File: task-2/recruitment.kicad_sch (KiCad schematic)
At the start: 0 parts

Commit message: Schema con partitori per le soglie, comparatori per i sensori e alimentazione del Lm393
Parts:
- added R1: 9.1k, symbol Device:R
- added R2: 4.7k, symbol Device:R
- added R3: 13k, symbol Device:R
- added R4: 15k, symbol Device:R
- added U1: LM393, symbol Comparator:LM393
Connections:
- new net BRAKE_SENS: U1.3 (+)
- new net CURR_SENS: U1.5 (+)
- new net GND: R2.2, R4.2, U1.4 (V-)
- new net VIN: U1.8 (V+)
- new net V_refBrake: R1.2, R2.1, U1.2 (-)
- new net V_refCurrent: R3.2, R4.1, U1.6 (-)

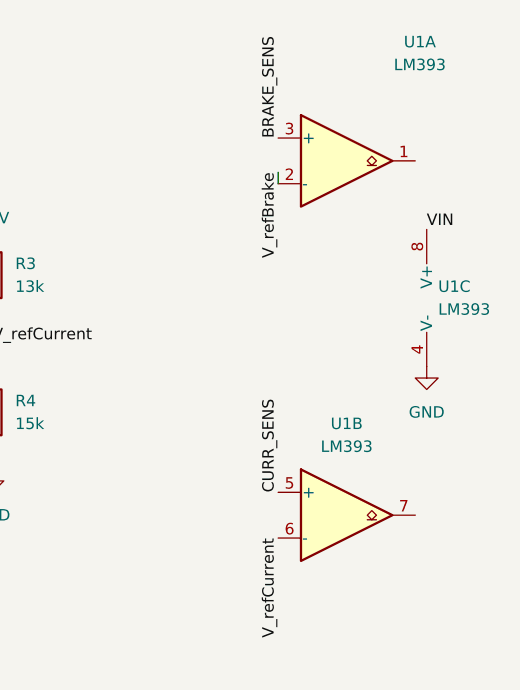
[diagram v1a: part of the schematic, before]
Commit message: Pullup e correzzione sulle resistenze r3 r4 per la seconda volta perche mi sono dimenticato di salvare su kicad
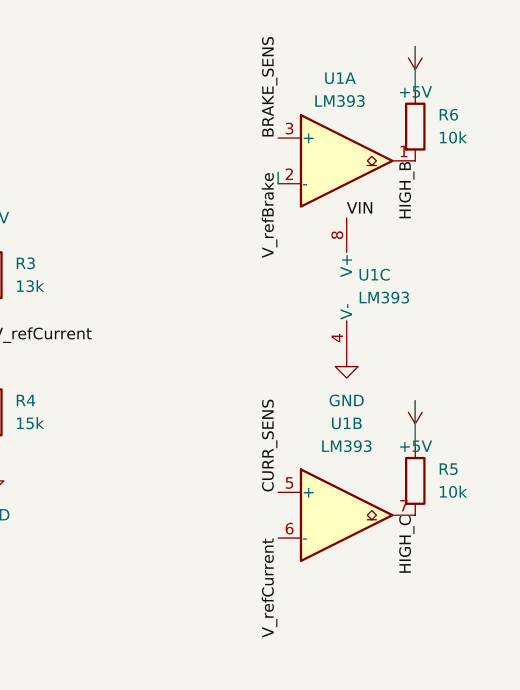
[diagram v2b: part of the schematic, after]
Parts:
- added R5, R6: 10k, symbol Device:R
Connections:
- net +5V: now also R5.1, R6.1
- net HIGH_B: now reaches U1.1
- net HIGH_B: now also R6.2
- net HIGH_C: now reaches U1.7
- net HIGH_C: now also R5.2
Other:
- moved on the sheet: U1C

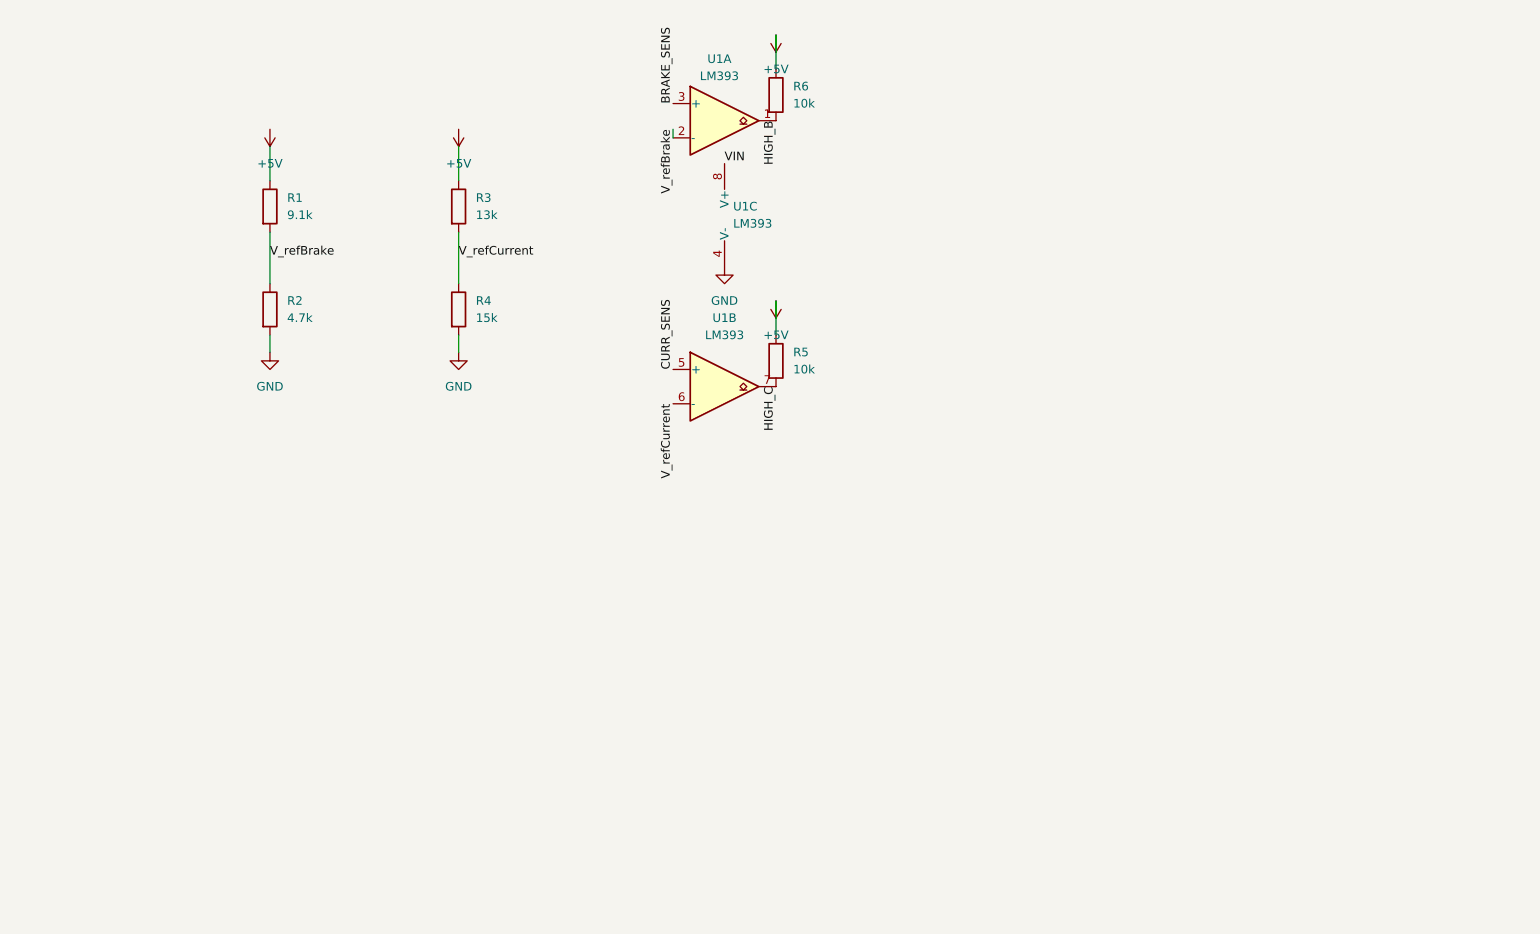
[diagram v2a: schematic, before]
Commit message: Beccare fail nei sensosi,pullup sugli ingressi, condensatori sul'alimentazione, aggiorno note
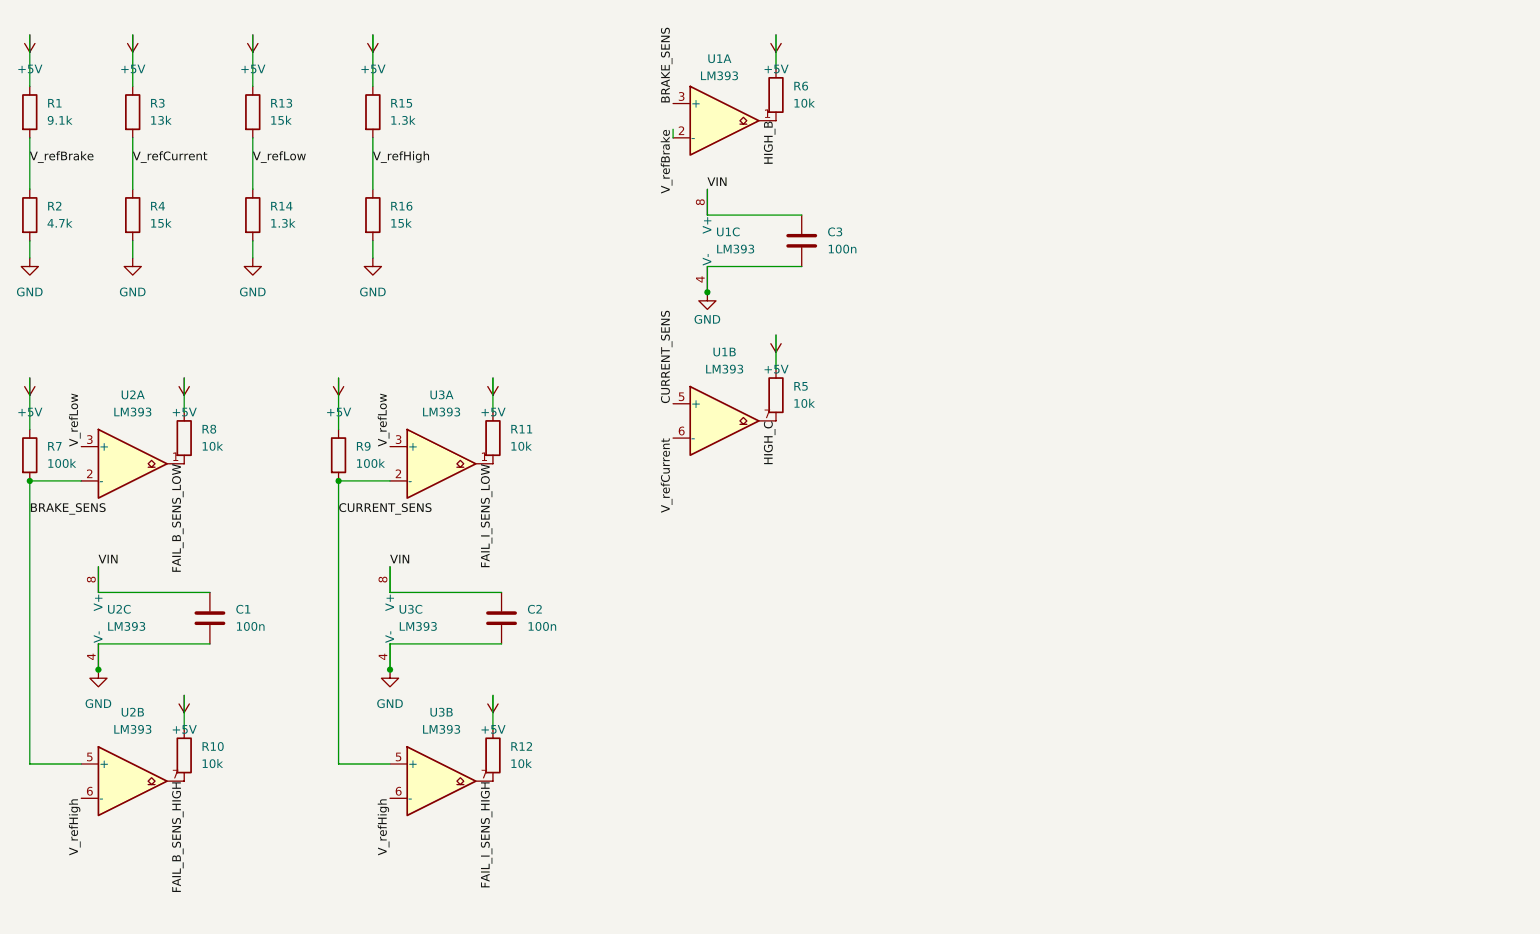
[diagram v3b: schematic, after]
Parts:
- added C1, C2, C3: 100n, symbol Device:C
- added R10, R11, R12, R8: 10k, symbol Device:R
- added R13, R16: 15k, symbol Device:R
- added R14, R15: 1.3k, symbol Device:R
- added R7, R9: 100k, symbol Device:R
- added U2, U3: LM393, symbol Comparator:LM393
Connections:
- net +5V: now also R1.1, R3.1, R10.1, R11.1, R12.1, R13.1, R15.1, R7.1, R8.1, R9.1
- net BRAKE_SENS: now also R7.2, U2.2 (-), U2.5 (+)
- net GND: now also C1.2, C2.2, C3.2, R14.2, R16.2, U2.4 (V-), U3.4 (V-)
- net VIN: now also C1.1, C2.1, C3.1, U2.8 (V+), U3.8 (V+)
- net CURR_SENS renamed CURRENT_SENS
- net CURRENT_SENS: now also R9.2, U3.2 (-), U3.5 (+)
- new net FAIL_B_SENS_HIGH: R10.2, U2.7
- new net FAIL_B_SENS_LOW: R8.2, U2.1
- new net FAIL_I_SENS_HIGH: R12.2, U3.7
- new net FAIL_I_SENS_LOW: R11.2, U3.1
- new net V_refHigh: R15.2, R16.1, U2.6 (-), U3.6 (-)
- new net V_refLow: R13.2, R14.1, U2.3 (+), U3.3 (+)
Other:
- moved on the sheet: R1, R2, R3, R4, R5, U1B, U1C

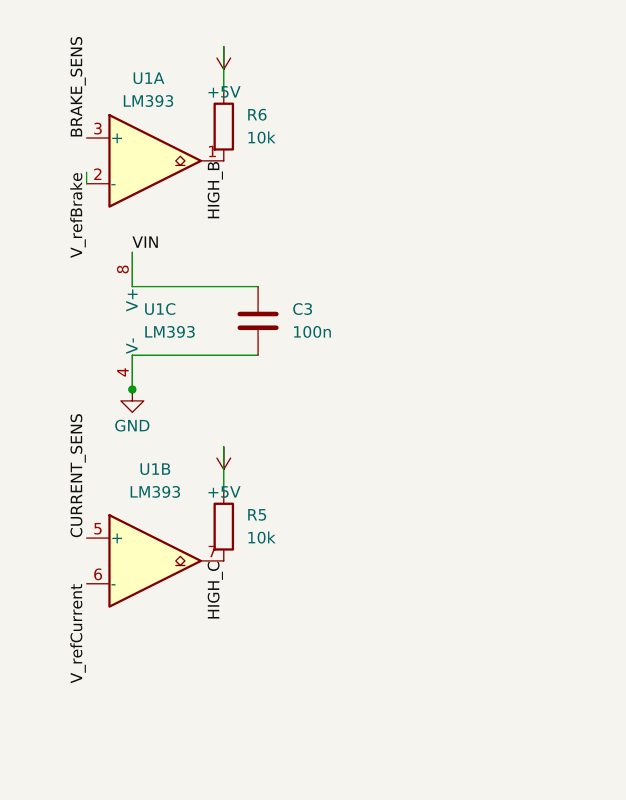
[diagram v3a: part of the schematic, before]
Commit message: Wired and sui comparatori U1A,U1B, elimitate e aggiunto resistenza con pullup, fuso i label per fare nodo unico per comparatori e pullup
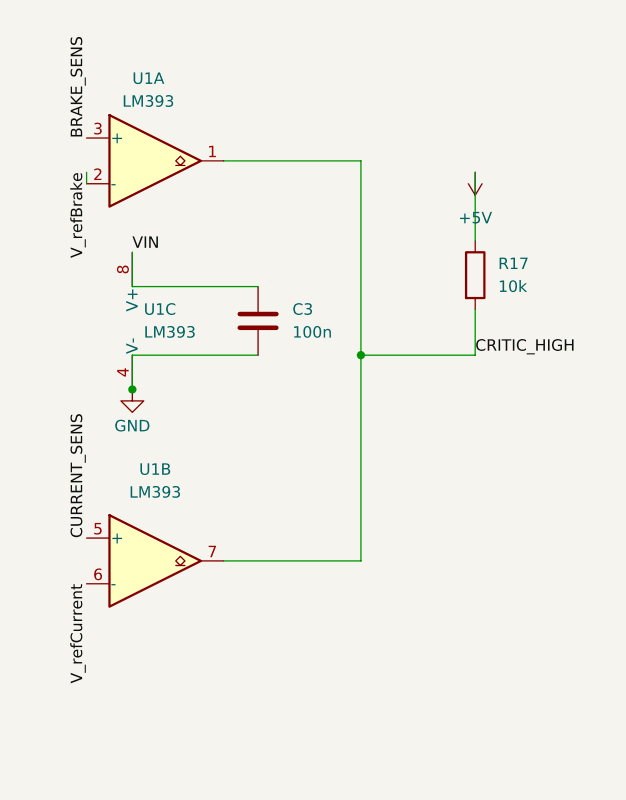
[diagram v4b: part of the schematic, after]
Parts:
- removed R5, R6: 10k, symbol Device:R
- added R17: 10k, symbol Device:R
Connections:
- net HIGH_C is gone; now on an unnamed net: U1.7
- net +5V: now also R17.1
- net HIGH_B: no longer names the net of U1.1
- net HIGH_B: now also R17.2

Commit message: Messo su carta il timer da 500ms,agginto capacitore(timer) e resistenza per la sua scarica
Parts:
- added C4: 47micro, symbol Device:C
- added R5: 1.5k, symbol Device:R
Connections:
- net at R17.2, U1.1, U1.7: now also R5.1
- new net: C4.1, R5.2
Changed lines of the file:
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@@
 	)
 	(junction
+		(at 156.21 50.8)
+		(diameter 0)
+		(color 0 0 0 0)
+	)
+	(junction
 		(at 118.11 54.61)
 		(diameter 0)
@@
 	(wire
 		(pts
+			(xy 156.21 50.8) (xy 170.18 50.8)
+		)
+		(stroke
+			(width 0)
+			(type default)
+		)
+	)
+	(wire
+		(pts
 			(xy 17.78 46.99) (xy 17.78 49.53)
 		)
@@
 	(wire
 		(pts
+			(xy 177.8 50.8) (xy 182.88 50.8)
+		)
+		(stroke
+			(width 0)
+			(type default)
+		)
+	)
+	(wire
+		(pts
 			(xy 33.02 31.75) (xy 33.02 39.37)
 		)
@@
 	(symbol
 		(lib_id "Device:R")
+		(at 173.99 50.8 90)
+		(unit 1)
+		(body_style 1)
+		(exclude_from_sim no)
+		(in_bom yes)
+		(on_board yes)
+		(in_pos_files yes)
+		(dnp no)
+		(fields_autoplaced yes)
+		(property "Reference" "R5"
+			(at 173.99 44.45 90)
+			(show_name no)
+			(do_not_autoplace no)
+			(effects
+				(font
+					(size 1.27 1.27)
+				)
+			)
+		)
+		(property "Value" "1.5k"
+			(at 173.99 46.99 90)
+			(show_name no)
+			(do_not_autoplace no)
+			(effects
+				(font
+					(size 1.27 1.27)
+				)
+			)
+		)
+		(property "Footprint" ""
+			(at 173.99 52.578 90)
+			(hide yes)
+			(show_name no)
+			(do_not_autoplace no)
+			(effects
+				(font
+					(size 1.27 1.27)
+				)
+			)
+		)
+		(property "Datasheet" ""
+			(at 173.99 50.8 0)
+			(hide yes)
+			(show_name no)
+			(do_not_autoplace no)
+			(effects
+				(font
+					(size 1.27 1.27)
+				)
+			)
+		)
+		(property "Description" "Resistor"
+			(at 173.99 50.8 0)
+			(hide yes)
+			(show_name no)
+			(do_not_autoplace no)
+			(effects
+				(font
+					(size 1.27 1.27)
+				)
+			)
+		)
+		(pin "2"
+		)
+		(pin "1"
+		)
+		(instances
+			(project "recruitment"
+				(path "/bdc7face-9f7c-4701-80bb-4cc144448db1"
+					(reference "R5")
+					(unit 1)
+				)
+			)
+		)
+	)
+	(symbol
+		(lib_id "Device:R")
 		(at 63.5 78.74 0)
 		(unit 1)
@@
 					(unit 1)
 				)
+			)
+		)
+	)
+	(symbol
+		(lib_id "Device:C")
+		(at 186.69 50.8 90)
+		(unit 1)
+		(body_style 1)
+		(exclude_from_sim no)
+		(in_bom yes)
+		(on_board yes)
+		(in_pos_files yes)
+		(dnp no)
+		(fields_autoplaced yes)
+		(property "Reference" "C4"
+			(at 186.69 43.18 90)
+			(show_name no)
+			(do_not_autoplace no)
+			(effects
+				(font
+					(size 1.27 1.27)
+				)
+			)
+		)
+		(property "Value" "47micro"
+			(at 186.69 45.72 90)
+			(show_name no)
+			(do_not_autoplace no)
+			(effects
+				(font
+					(size 1.27 1.27)
+				)
+			)
+		)
+		(property "Footprint" ""
+			(at 190.5 49.8348 0)
+			(hide yes)
+			(show_name no)
+			(do_not_autoplace no)
+			(effects
+				(font
+					(size 1.27 1.27)
+				)
+			)
+		)
+		(property "Datasheet" ""
+			(at 186.69 50.8 0)
+			(hide yes)
+			(show_name no)
+			(do_not_autoplace no)
+			(effects
+				(font
+					(size 1.27 1.27)
+				)
+			)
+		)
+		(property "Description" "Unpolarized capacitor"
+			(at 186.69 50.8 0)
+			(hide yes)
+			(show_name no)
+			(do_not_autoplace no)
+			(effects
+				(font
+					(size 1.27 1.27)
+				)
+			)
+		)
+		(pin "2"
+		)
+		(pin "1"
+		)
+		(instances
+			(project "recruitment"
+				(path "/bdc7face-9f7c-4701-80bb-4cc144448db1"
+					(reference "C4")
+					(unit 1)
+				)

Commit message: creato il timer per l'apertura del rele'ed un partirore di tesione per la soglia del timer
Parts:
- added C5: 100n, symbol Device:C
- added R18: 6.5k, symbol Device:R
- added R19: 10k, symbol Device:R
- added U4: LM393, symbol Comparator:LM393
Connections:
- net +5V: now also R18.1
- net GND: now also C5.2, R19.2, U4.4 (V-)
- net VIN: now also C5.1, U4.8 (V+)
- net at C4.2: now also U4.3 (+)
- new net V_refTimer: R18.2, R19.1, U4.2 (-)

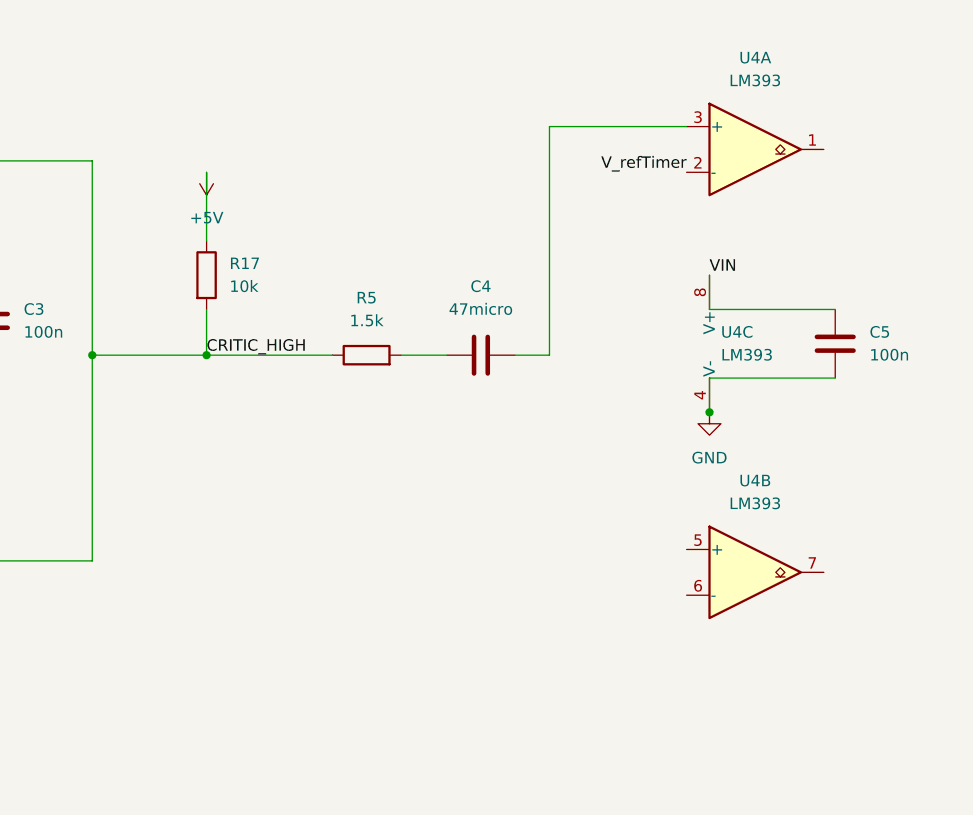
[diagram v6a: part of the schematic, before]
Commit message: latch del guasto con retroazione positiva e corretto il conensatore c4
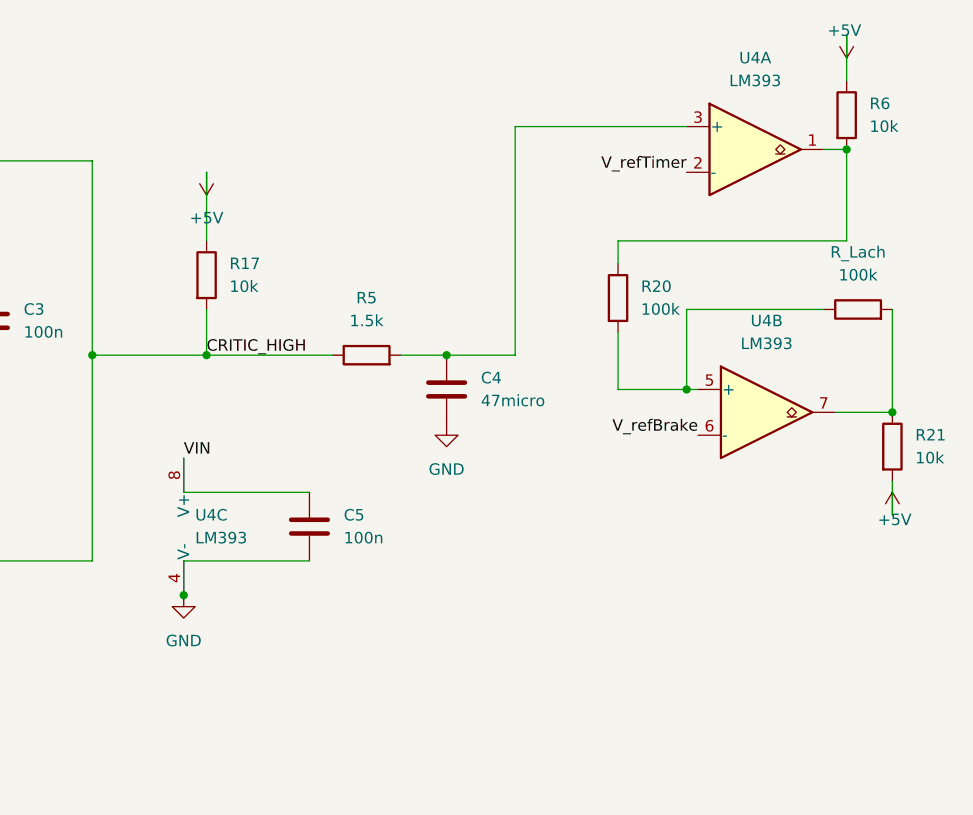
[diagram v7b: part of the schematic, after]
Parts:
- added R20, R_Lach: 100k, symbol Device:R
- added R21, R6: 10k, symbol Device:R
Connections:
- net +5V: now also R21.2, R6.1
- net GND: now also C4.1
- net V_refBrake: now also U4.6 (-)
- net at U4.5 (+): now also R20.2, R_Lach.1
- net at U4.7: now also R21.1, R_Lach.2
- net at R5.2: now also C4.2, U4.3 (+); no longer C4.1
- net at U4.1: now also R20.1, R6.2
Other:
- moved on the sheet: C4, C5, U4B, U4C
